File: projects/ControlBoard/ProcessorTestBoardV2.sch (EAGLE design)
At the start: 87 parts

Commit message: Top and Side Panels, Proc Test Board prepared for production
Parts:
- added LED-IR, LED3V3, LED3V6, LED5V: (no value), CNTRL_BOARD:RESISTOR
- added R31: 560R, CNTRL_BOARD:RESISTOR
- added R36, R40, R41, R42: 0R, CNTRL_BOARD:RESISTOR
- added R37, R38: 250R, CNTRL_BOARD:RESISTOR
- added R39: 330R, CNTRL_BOARD:RESISTOR
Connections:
- removed net PA10: SAMD21J.PA10
- new net N$16: LED-IR.2, R38.1
- new net N$21: LED3V6.2, R39.1
- new net N$22: LED5V.2, R31.1
- new net N$23: LED3V3.2, R37.1
- new net PA20[2]: SAMD21J.PA20
- new net PA21[3]: SAMD21J.PA21
- new net PA22: SAMD21J.PA22
- new net PA23: SAMD21J.PA23
- new net PA24: SAMD21J.PA24
- new net PA25: SAMD21J.PA25
- new net PAD[0]: SAMD21J.PA04
- new net PAD[1]: SAMD21J.PA05
- new net PB02: SAMD21J.PB02
- new net PB03: SAMD21J.PB03
- new net PB16: SAMD21J.PB16
- new net PB17: SAMD21J.PB17
- net 3V3: now also R36.1, R36.2, R37.2, R40.1, R40.2, R41.1, R41.2, R42.1, R42.2
- net 3V6: now also R39.2
- net 5V: now also R31.2
- net GND: now also LED-IR.1, LED3V3.1, LED3V6.1, LED5V.1
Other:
- note added: "0 ohm resistors to fix routing"
- note removed: "Test Output"

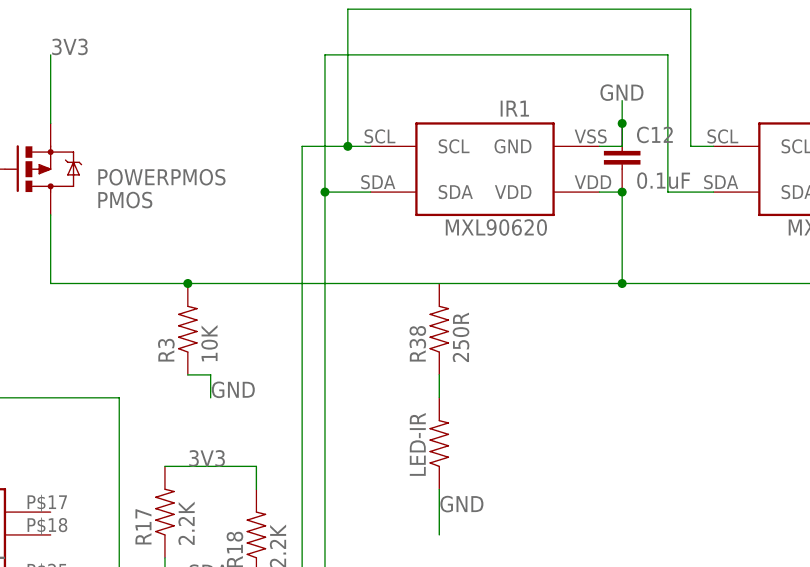
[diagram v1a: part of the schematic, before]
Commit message: Started Battery Board and fixes to library
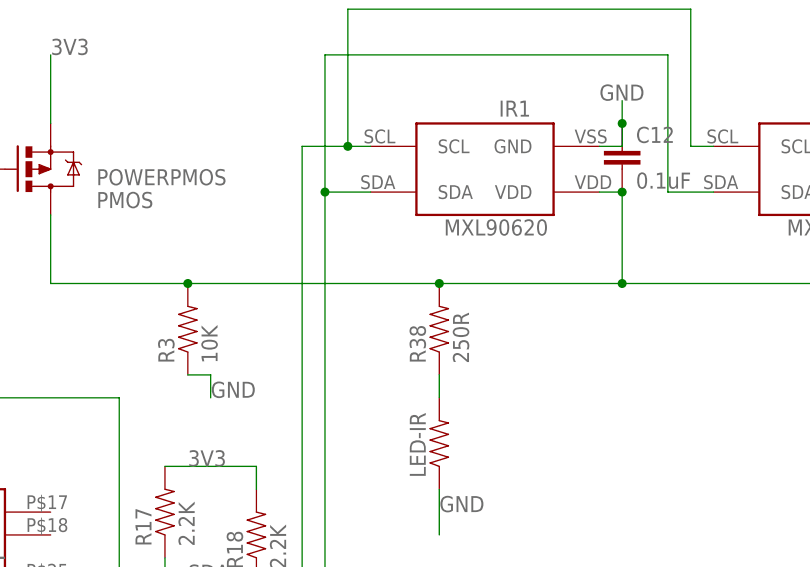
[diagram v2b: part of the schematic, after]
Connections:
- net N$1: now also R38.2
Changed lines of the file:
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@@
 <wire x1="55.88" y1="157.48" x2="55.88" y2="149.86" width="0.1524" layer="91"/>
 <wire x1="55.88" y1="149.86" x2="71.12" y2="149.86" width="0.1524" layer="91"/>
-<wire x1="71.12" y1="149.86" x2="119.38" y2="149.86" width="0.1524" layer="91"/>
+<wire x1="71.12" y1="149.86" x2="99.06" y2="149.86" width="0.1524" layer="91"/>
+<wire x1="99.06" y1="149.86" x2="119.38" y2="149.86" width="0.1524" layer="91"/>
 <wire x1="119.38" y1="149.86" x2="119.38" y2="160.02" width="0.1524" layer="91"/>
 <pinref part="IR1" gate="G$1" pin="VDD"/>
@@
 <pinref part="R3" gate="G$1" pin="2"/>
 <junction x="71.12" y="149.86"/>
+<pinref part="R38" gate="G$1" pin="2"/>
+<junction x="99.06" y="149.86"/>
 </segment>
 </net>
